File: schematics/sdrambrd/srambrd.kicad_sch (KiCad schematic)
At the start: 24 parts, among them J1 LEFT, J2 Micro_SD_Card, J3 Conn_01x03, J4 Conn_01x03, U1 IS61LV25616AL

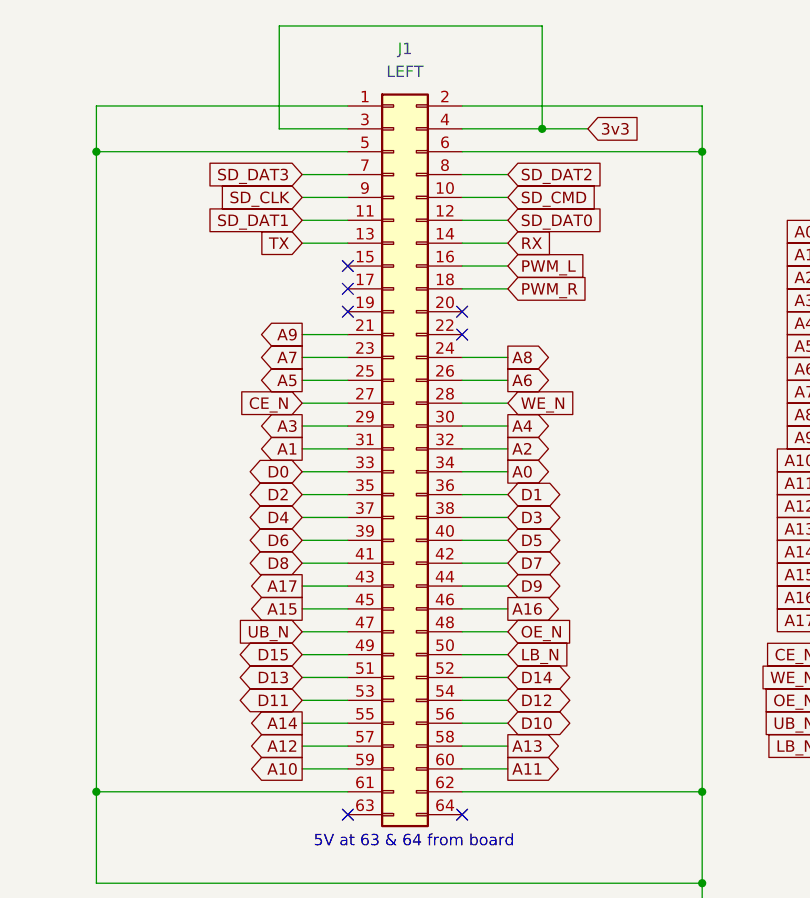
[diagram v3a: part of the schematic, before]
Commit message: Rv32: Another revision of the AUX board, ordered from JLCPCB.
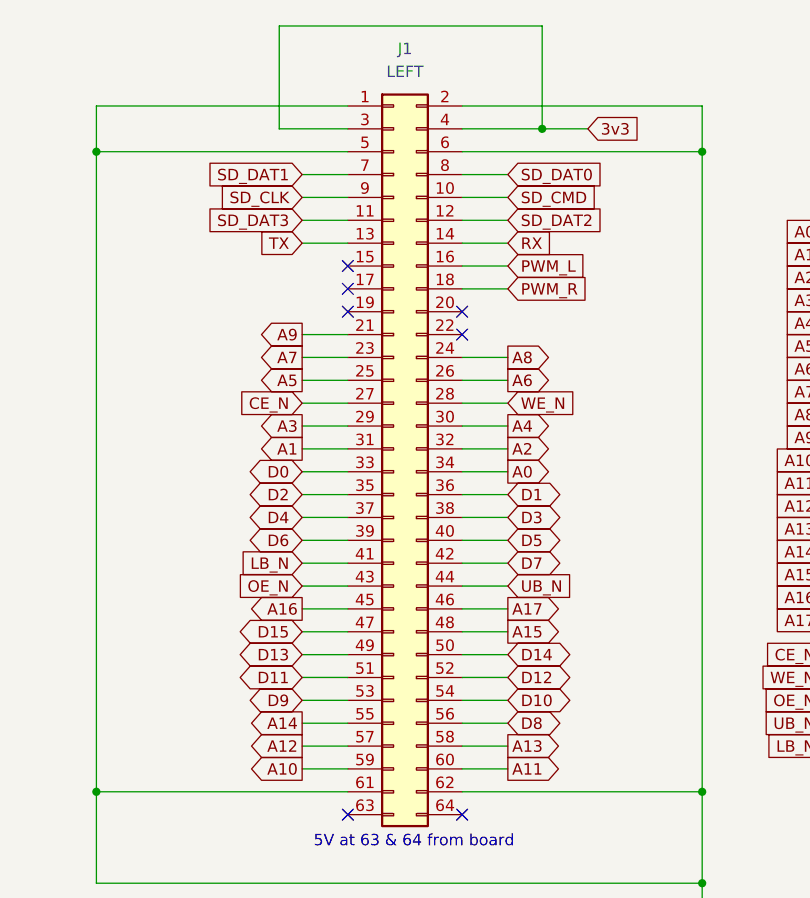
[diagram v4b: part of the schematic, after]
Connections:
- net A15: now also J1.48 (Pin_48); no longer J1.45 (Pin_45)
- net A16: now also J1.45 (Pin_45); no longer J1.46 (Pin_46)
- net A17: now also J1.46 (Pin_46); no longer J1.43 (Pin_43)
- net D10: now also J1.54 (Pin_54); no longer J1.56 (Pin_56)
- net D11: now also J1.51 (Pin_51); no longer J1.53 (Pin_53)
- net D12: now also J1.52 (Pin_52); no longer J1.54 (Pin_54)
- net D13: now also J1.49 (Pin_49); no longer J1.51 (Pin_51)
- net D14: now also J1.50 (Pin_50); no longer J1.52 (Pin_52)
- net D15: now also J1.47 (Pin_47); no longer J1.49 (Pin_49)
- net D8: now also J1.56 (Pin_56); no longer J1.41 (Pin_41)
- net D9: now also J1.53 (Pin_53); no longer J1.44 (Pin_44)
- net LB_N: now also J1.41 (Pin_41); no longer J1.50 (Pin_50)
- net OE_N: now also J1.43 (Pin_43); no longer J1.48 (Pin_48)
- net SD_DAT0: now also J1.8 (Pin_8); no longer J1.12 (Pin_12)
- net SD_DAT1: now also J1.7 (Pin_7); no longer J1.11 (Pin_11)
- net SD_DAT2: now also J1.12 (Pin_12); no longer J1.8 (Pin_8)
- net SD_DAT3: now also J1.11 (Pin_11); no longer J1.7 (Pin_7)
- net UB_N: now also J1.44 (Pin_44); no longer J1.47 (Pin_47)
